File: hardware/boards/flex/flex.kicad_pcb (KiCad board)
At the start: 2 copper layers, 23.1 x 12.5 mm, 2 parts, among them J1 Tail, J2 Tail

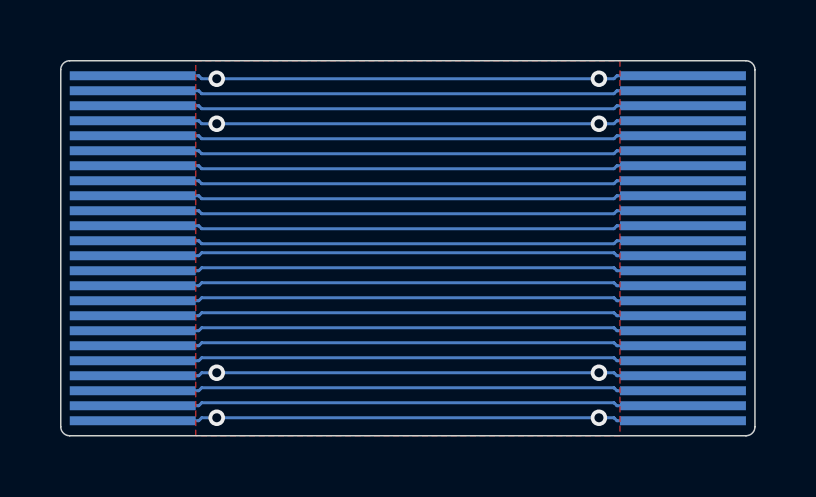
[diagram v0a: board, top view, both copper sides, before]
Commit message: feat(flex): loop the side-link flex between vertical FH12 connectors
18.4 mm end to end, fingers exposed 2.5 mm and a 0.225 mm PI stiffener to 4.2 mm from each tip (0.34 mm at the fingers against the FH12's 0.35 +/-0.03). Fitted bent 180 degrees at about 2.5 mm radius over a 1.5 mm board gap.
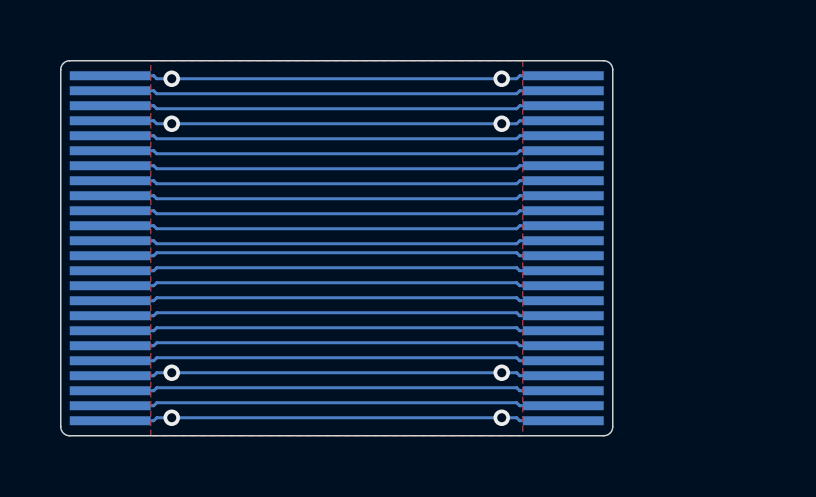
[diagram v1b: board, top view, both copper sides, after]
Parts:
- moved J1 4.74 mm to (118.4, 106.2)
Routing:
- net GND: track 58.5 -> 51.5 mm
- net Net-(J1-Pin_9): track 14.6 -> 12.9 mm
- net Net-(J1-Pin_8): track 14.6 -> 12.9 mm
- net Net-(J1-Pin_7): track 14.6 -> 12.9 mm
- net Net-(J1-Pin_6): track 14.6 -> 12.9 mm
- net Net-(J1-Pin_5): track 14.6 -> 12.9 mm
- net Net-(J1-Pin_3): track 14.6 -> 12.9 mm
- net Net-(J1-Pin_23): track 14.6 -> 12.9 mm
- net Net-(J1-Pin_22): track 14.6 -> 12.9 mm
- net Net-(J1-Pin_20): track 14.6 -> 12.9 mm
- net Net-(J1-Pin_2): track 14.6 -> 12.9 mm
- net Net-(J1-Pin_19): track 14.6 -> 12.9 mm
- net Net-(J1-Pin_18): track 14.6 -> 12.9 mm
- net Net-(J1-Pin_17): track 14.6 -> 12.9 mm
- net Net-(J1-Pin_16): track 14.6 -> 12.9 mm
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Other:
- board size 23.1 x 12.5 mm -> 18.4 x 12.5 mm
- board text added: "JLC two-layer polyimide flex, 0.19 mm: 50 um PI core, 18 um copper, ENIG; yellow coverlay, 25 um PI + 25 um adhesive, both sides. The bottom coverlay opens 2.5 mm from each tip over the fingers. No silkscreen. PI stiffener 0.225 mm on the top over each end, outline on User.1 Stiffener, 4.2 mm from each tip: 0.34 mm at the fingers. Laser outline +/-0.05 mm: tails 12.50 +/-0.05 mm wide for Hirose F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"
- board text removed: "JLC two-layer polyimide flex, 0.19 mm: 50 um PI core, 18 um copper, ENIG; yellow coverlay, 25 um PI + 25 um adhesive, both sides. The bottom coverlay opens 4.0 mm from each tip over the fingers. No silkscreen. PI stiffener 0.20 mm on the top over each end, outline on User.1 Stiffener, 6.0 mm from each tip: 0.32 mm at the fingers. Laser outline +/-0.05 mm: tails 12.50 +/-0.05 mm wide for HanElectr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"
